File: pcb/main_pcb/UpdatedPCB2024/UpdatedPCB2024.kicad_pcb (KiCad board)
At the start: 2 copper layers, 97.8 x 78.1 mm, 31 parts, among them J1 Conn_01x05, J10 Screw_Terminal_01x02, J2 Conn_01x05, J3 Conn_01x05, J4 Conn_01x05, J5 Conn_01x05, J6 Conn_01x05, J7 Conn_01x05, J8 Conn_01x06_Male, J9 Conn_01x06_Male, Q1 Q_NJFET_DSG, Q2 Q_NJFET_DSG, SW1 SW_SPDT, U1 Teensy_4.0, U2 DRV8833, U3 LM3151/2/3

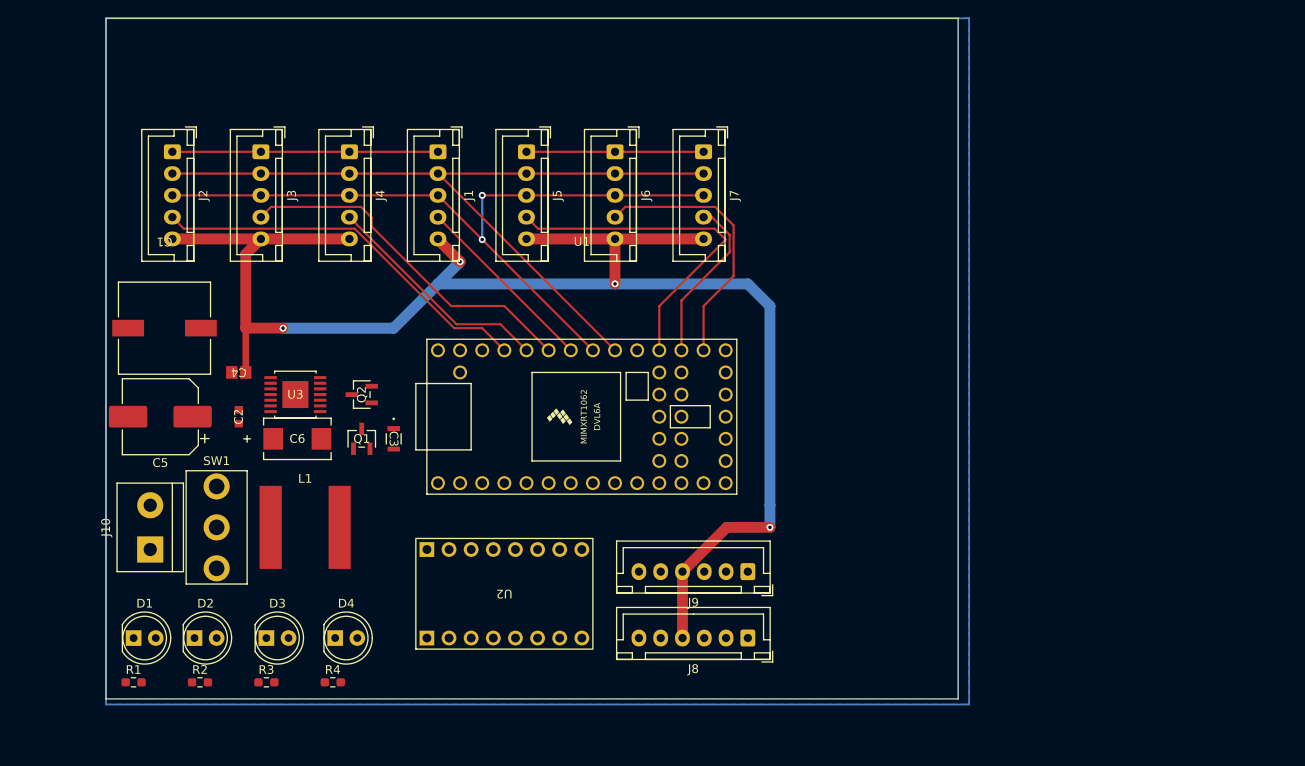
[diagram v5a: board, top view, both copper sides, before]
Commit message: Routing done, DRC pass
Finsihed layout and routing, filled ground plane, and added vias to tie off ground plane.
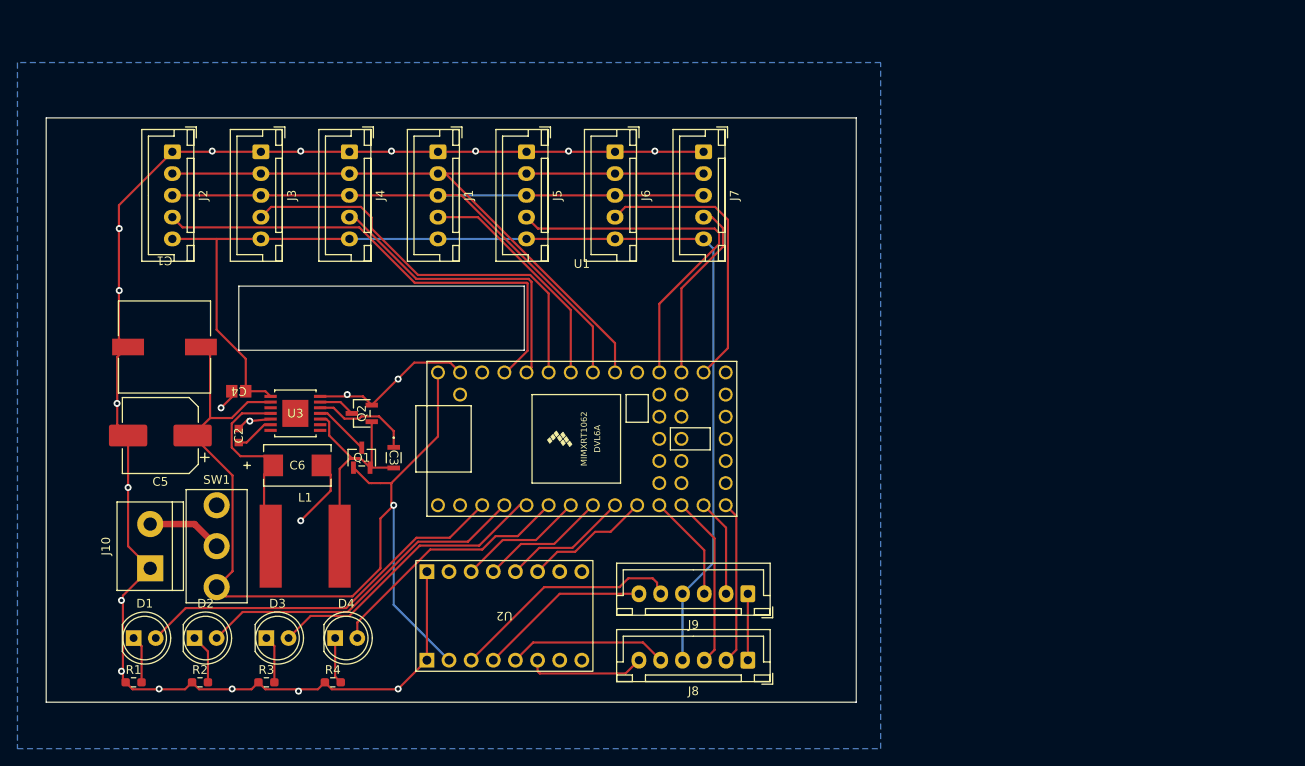
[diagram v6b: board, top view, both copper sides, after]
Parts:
- moved C6 3.05 mm to (108.3, 109.7)
- moved J8 2.54 mm to (160.0, 132.1)
- moved U1 2.54 mm to (141.0, 106.7)
- moved U2 2.54 mm to (132.1, 127.0)
- moved J9 2.54 mm to (160.0, 124.5)
- moved J10 2.16 mm to (91.4, 121.5)
- moved Q2 2.16 mm to (115.7, 103.8)
- moved U3 2.16 mm to (108.1, 103.8)
- moved C1 2.16 mm to (93.1, 96.1)
- moved C2 2.16 mm to (101.6, 106.3)
- moved C3 2.16 mm to (119.4, 108.8)
- moved C4 2.16 mm to (101.6, 101.2)
- moved C5 2.16 mm to (92.6, 106.3)
- moved L1 2.16 mm to (109.2, 119.0)
- moved Q1 2.16 mm to (115.7, 108.8)
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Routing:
- net GND: track 50.8 -> 219.5 mm, vias 0 -> 21
- net +BATT: track 0.00 -> 110.7 mm, vias 0 -> 1
- net +3V3: track 177.6 -> 133.2 mm, vias 4 -> 0
- net /LED0: track 0.00 -> 43.8 mm
- net /LED1: track 0.00 -> 39.3 mm
- net /LED2: track 0.00 -> 33.6 mm
- net /LED3: track 0.00 -> 29.3 mm
- net Net-(Q1-S): track 0.00 -> 28.9 mm
- net /BOUT1: track 0.00 -> 26.9 mm
- net Net-(U3-FB): track 0.00 -> 23.3 mm
- net /BOUT2: track 0.00 -> 19.9 mm
- net /AEQ1: track 0.00 -> 19.8 mm
- net /AEQ2: track 0.00 -> 18.8 mm
- net /AOUT2: track 0.00 -> 18.4 mm
- net /AIN1: track 0.00 -> 14.6 mm
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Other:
- board size 97.8 x 78.1 mm -> 93 x 67.1 mm

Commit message: Generated Gerber file and finished board
Its done! yippeeee!
Added some holes, made some routes thicker, reran the filling functions etc. etc.
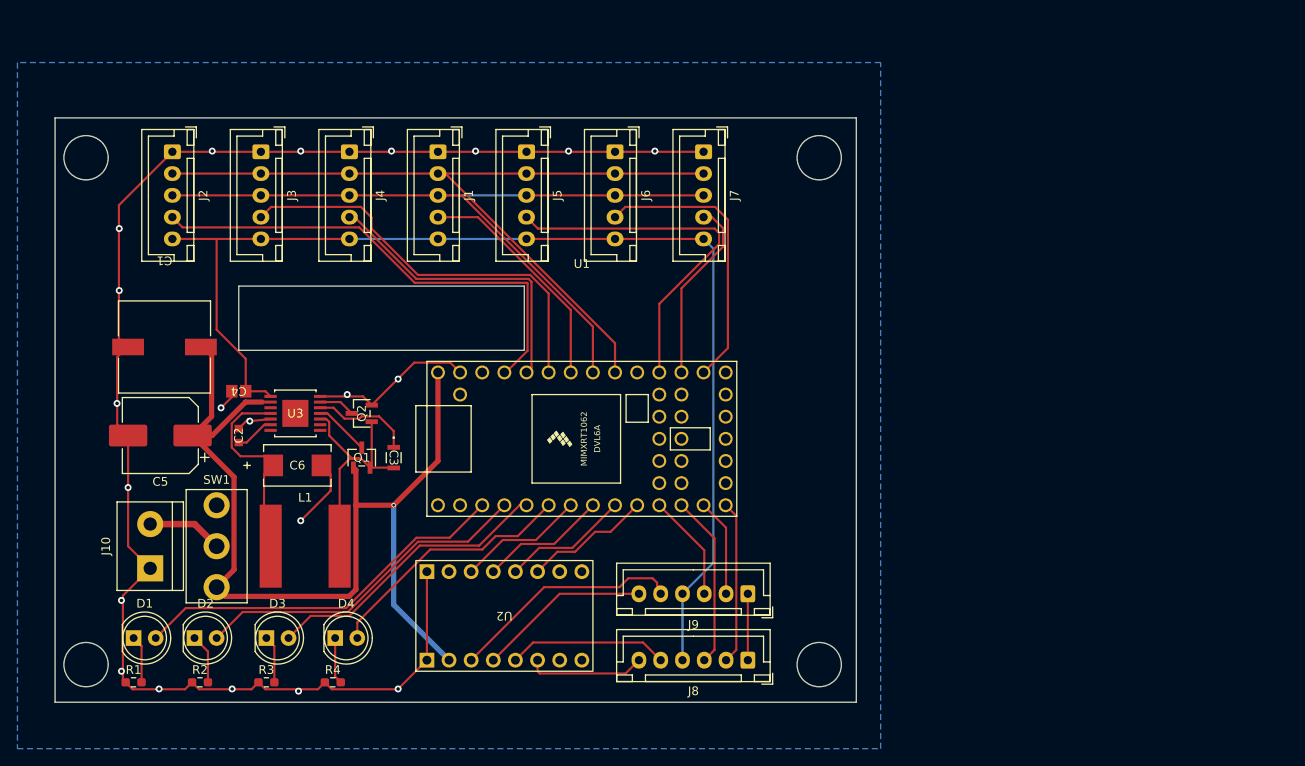
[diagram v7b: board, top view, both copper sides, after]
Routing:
- net +BATT: track 110.7 -> 114.5 mm
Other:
- board size 93 x 67.1 mm -> 91.9 x 67.1 mm
